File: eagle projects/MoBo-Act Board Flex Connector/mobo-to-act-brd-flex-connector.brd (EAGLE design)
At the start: 40.6 x 137.8 mm, 2 parts

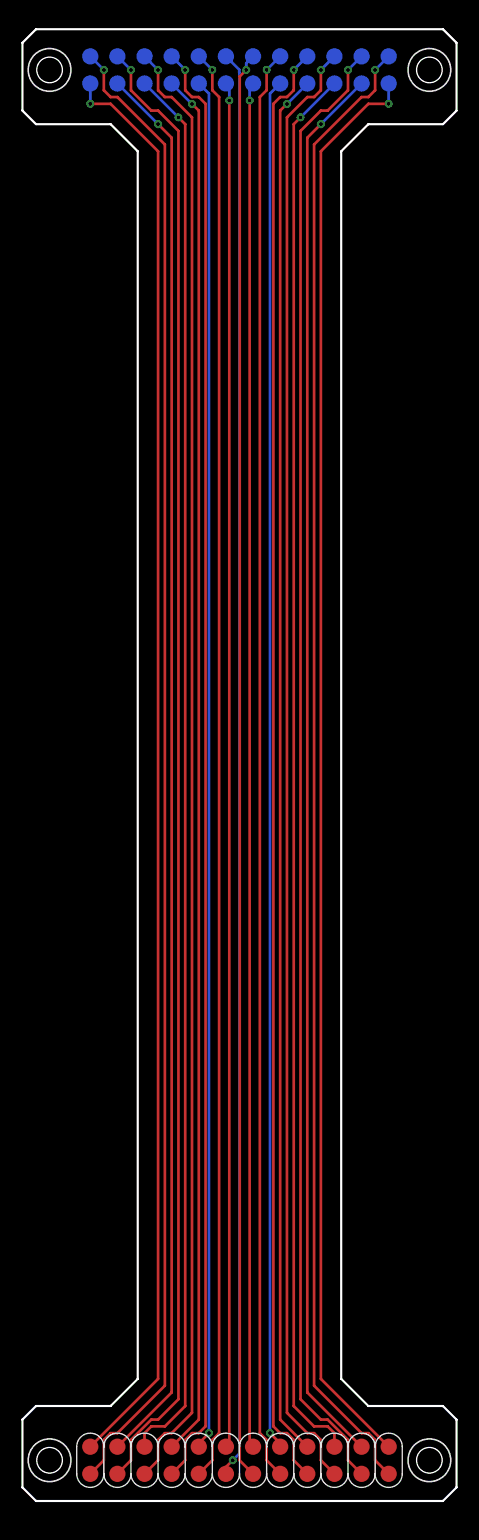
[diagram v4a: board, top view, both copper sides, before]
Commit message: Fixed Connector Boards
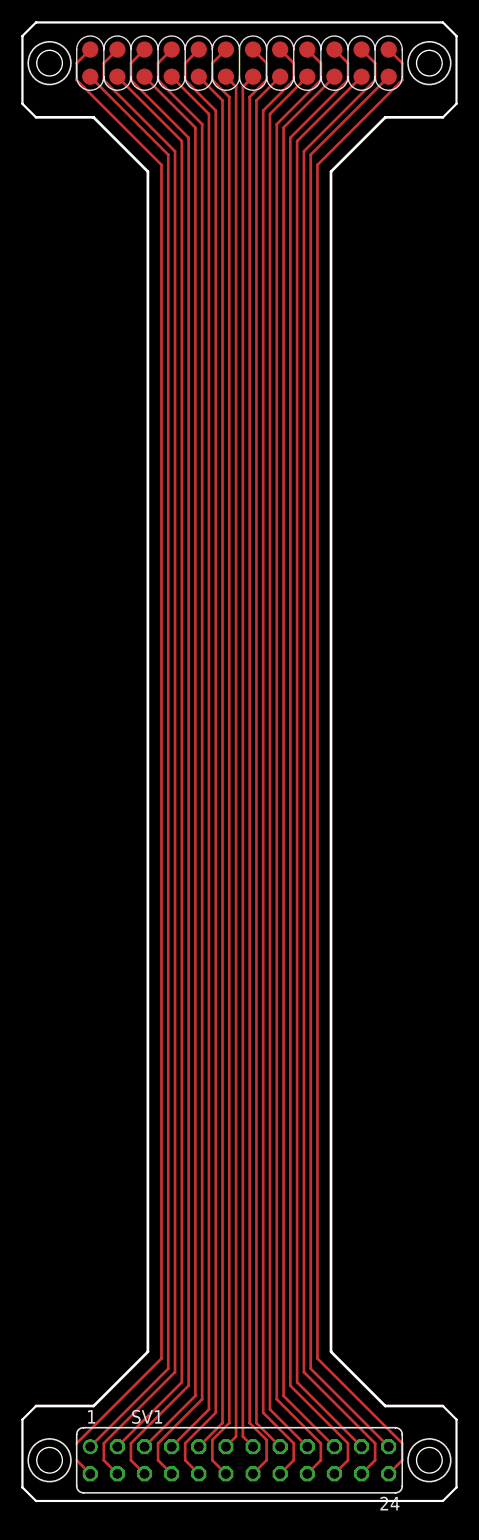
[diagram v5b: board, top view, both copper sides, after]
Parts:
- removed U$1: 12X2_SMD_2.54MM_HEADER, SMD_headers:12X2_HEADER
- added SV1: (no value), con-lsta:FE12-2
- U$2: value 12X2_MIRRORED_SMD_2.54MM_HEADER -> 12X2_SMD_2.54MM_HEADER
- moved U$2 0.63 mm to (26.7, 139.7), flipped to the top, turned to 0 degrees
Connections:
- net N$1: now also SV1.1, U$2.X12; no longer U$1.X1, U$2.X1
- net N$10: now also SV1.16, U$2.X20; no longer U$1.X10, U$2.X10
- net N$11: now also SV1.18, U$2.X21; no longer U$1.X11, U$2.X11
- net N$12: now also SV1.20, U$2.X22; no longer U$1.X12, U$2.X12
- net N$13: now also SV1.22, U$2.X23; no longer U$1.X24, U$2.X24
- net N$14: now also SV1.24, U$2.X24; no longer U$1.X23, U$2.X23
- net N$15: now also SV1.3, U$2.X11; no longer U$1.X22, U$2.X22
- net N$16: now also SV1.5, U$2.X10; no longer U$1.X21, U$2.X21
- net N$17: now also SV1.21, U$2.X2; no longer U$1.X20, U$2.X20
- net N$18: now also SV1.19, U$2.X3; no longer U$1.X19, U$2.X19
- net N$19: now also SV1.7, U$2.X9; no longer U$1.X18, U$2.X18
- net N$2: now also SV1.23, U$2.X1; no longer U$1.X2, U$2.X2
- net N$20: now also SV1.17, U$2.X4; no longer U$1.X17, U$2.X17
- net N$21: now also SV1.9, U$2.X8; no longer U$1.X16, U$2.X16
- net N$22: now also SV1.15, U$2.X5; no longer U$1.X15, U$2.X15
- net N$23: now also SV1.13, U$2.X6; no longer U$1.X14, U$2.X14
- net N$24: now also SV1.11, U$2.X7; no longer U$1.X13, U$2.X13
- net N$3: now also SV1.2, U$2.X13; no longer U$1.X3, U$2.X3
- net N$4: now also SV1.4, U$2.X14; no longer U$1.X4, U$2.X4
- net N$5: now also SV1.6, U$2.X15; no longer U$1.X5, U$2.X5
- net N$6: now also SV1.8, U$2.X16; no longer U$1.X6, U$2.X6
- net N$7: now also SV1.10, U$2.X17; no longer U$1.X7, U$2.X7
- net N$8: now also SV1.12, U$2.X18; no longer U$1.X8, U$2.X8
- net N$9: now also SV1.14, U$2.X19; no longer U$1.X9, U$2.X9
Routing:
- net N$14: track 131.8 -> 141.0 mm, vias 1 -> 0
- net N$13: track 134.0 -> 139.9 mm, vias 1 -> 0
- net N$24: track 134.0 -> 129.1 mm, vias 1 -> 0
- net N$1: track 139.2 -> 134.3 mm, vias 1 -> 0
- net N$17: track 128.4 -> 133.3 mm, vias 1 -> 0
- net N$5: track 134.3 -> 138.9 mm, vias 1 -> 0
- net N$18: track 127.9 -> 132.2 mm, vias 1 -> 0
- net N$6: track 133.7 -> 137.8 mm, vias 1 -> 0
- net N$2: track 138.2 -> 134.3 mm, vias 1 -> 0
- net N$4: track 136.1 -> 139.9 mm, vias 1 -> 0
- net N$19: track 127.9 -> 131.2 mm, vias 1 -> 0
- net N$7: track 133.8 -> 136.8 mm, vias 1 -> 0
- net N$23: track 131.8 -> 129.1 mm, vias 1 -> 0
- net N$20: track 128.4 -> 131.2 mm, vias 1 -> 0
- net N$16: track 129.8 -> 132.2 mm, vias 1 -> 0
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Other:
- board size 40.6 x 137.8 mm -> 40.6 x 138.4 mm
